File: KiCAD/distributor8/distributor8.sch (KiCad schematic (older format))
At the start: 52 parts, among them P1 CONN_02X03, P10 CONN_02X03, P11 CONN_02X03, P12 CONN_02X03, P13 CONN_02X03, P14 CONN_02X03, P15 CONN_02X03, P16 CONN_02X03, P17 CONN_02X03, P18 CONN_02X03, P19 CONN_02X03, P2 CONN_02X03, P20 CONN_02X03, P21 CONN_02X07, P22 CONN_02X07, P23 CONN_02X07, P24 CONN_02X07, P25 CONN_02X03, P26 CONN_02X03, P27 CONN_02X07, P28 CONN_02X07, P29 CONN_02X07, P3 CONN_02X03, P30 CONN_02X07, P31 CONN_02X03, P32 CONN_02X03, P33 CONN_02X03, P34 CONN_02X03, P35 CONN_02X07, P36 CONN_02X07, P37 CONN_02X07, P38 CONN_02X07, P39 CONN_02X03, P4 CONN_02X03, P40 CONN_02X03, P41 CONN_02X03, P42 CONN_02X03, P43 CONN_02X07, P44 CONN_02X07, P45 CONN_02X07, P46 CONN_02X07, P47 CONN_02X03, P48 CONN_02X03, P5 CONN_02X03, P6 CONN_02X03, P7 CONN_02X03, P8 CONN_02X03, P9 CONN_02X03

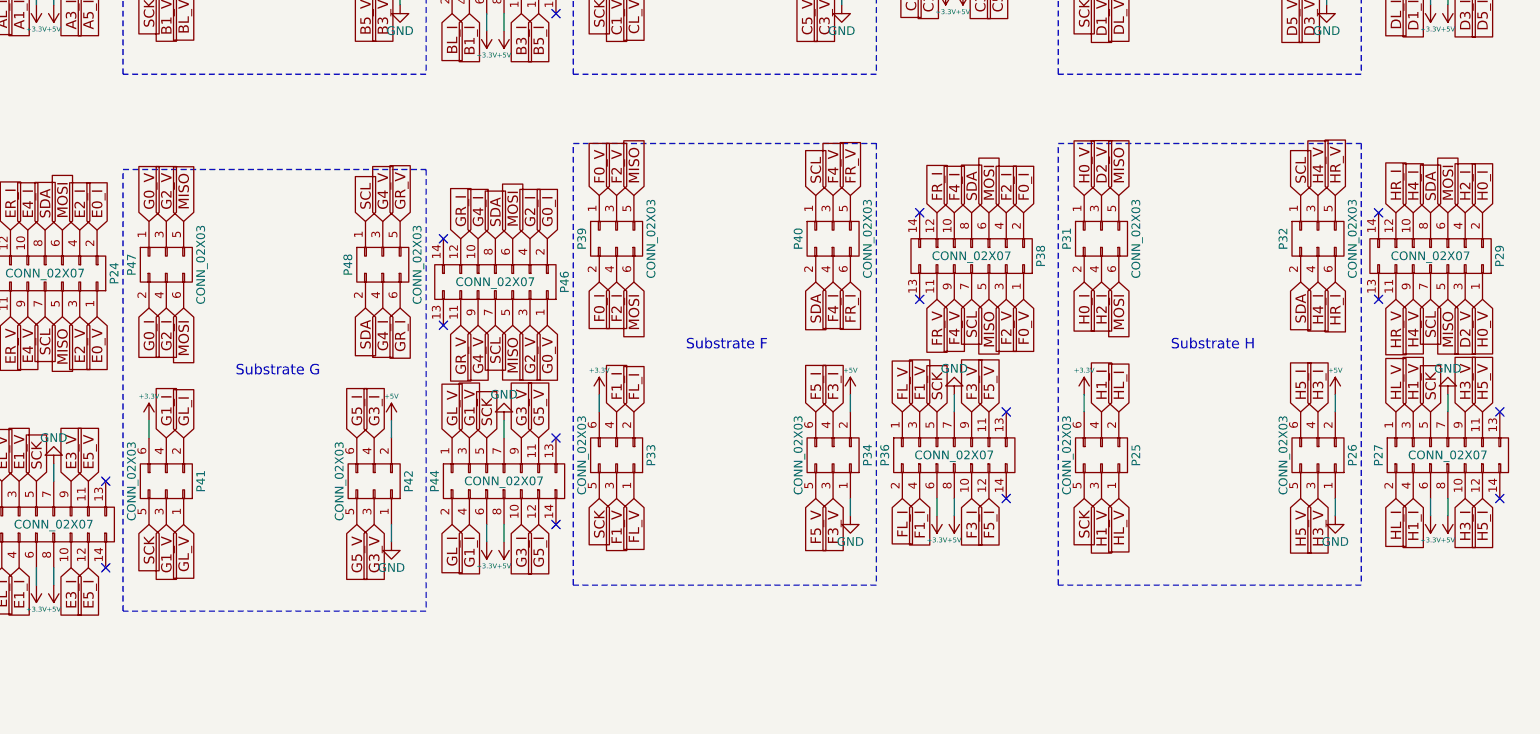
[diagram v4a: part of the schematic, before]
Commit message: try to fix messed up d8 routing
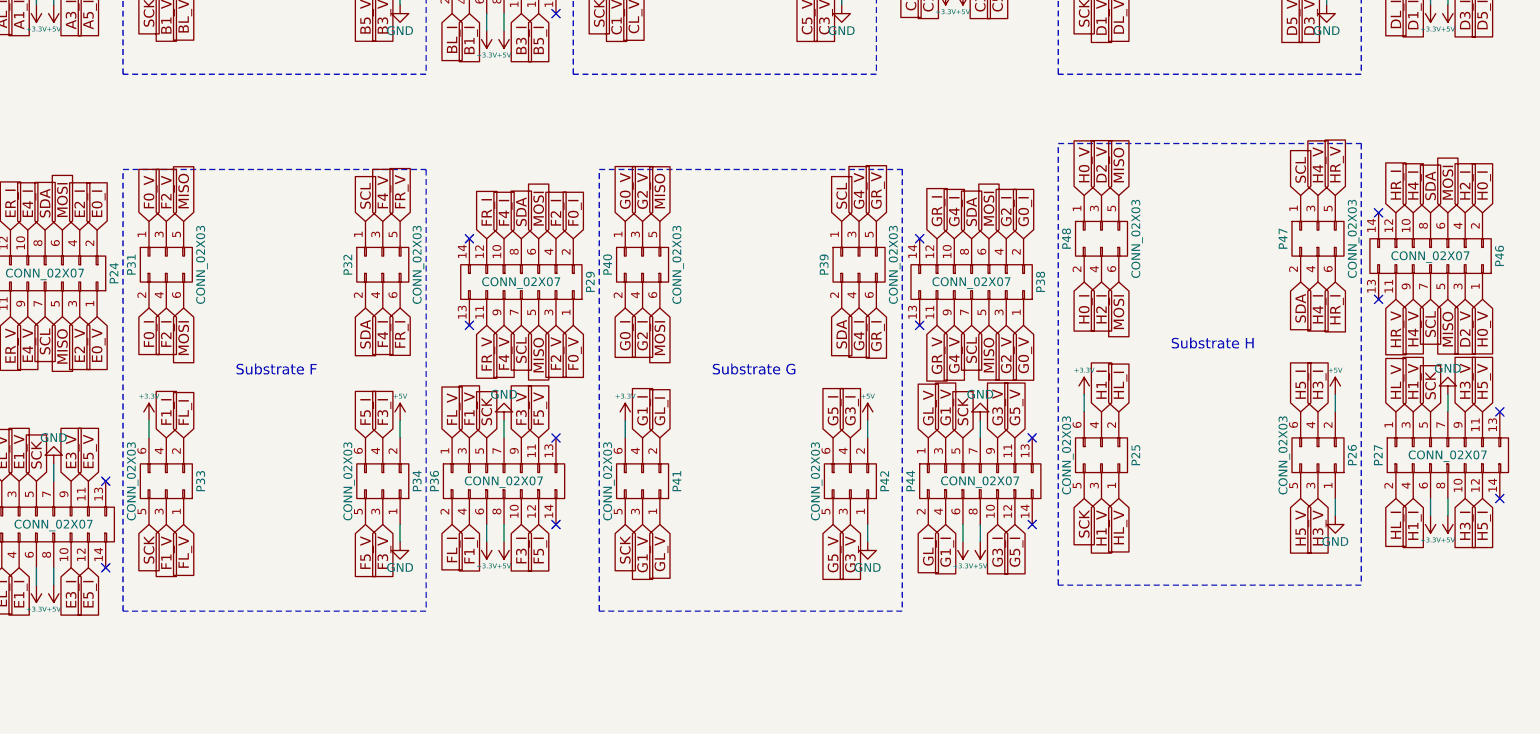
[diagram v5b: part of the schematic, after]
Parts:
- P40: renamed from P47; footprint myParts:SSW-107-02-T-D-RA -> myParts:TMS-103-01-L-D-SE
- renumbered P38 to P29, P39 to P31, P40 to P32, P46 to P38, P48 to P39, P29 to P46, P32 to P47, P31 to P48
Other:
- moved on the sheet: P29, P31, P32, P33, P34, P36, P38, P39, P40, P41, P42, P44

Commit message: fixed d8
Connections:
- net D2_V: no longer P46.3 (P3), P48.3 (P3)
- new net H2_V: P46.3 (P3), P48.3 (P3)
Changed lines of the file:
@@
 H0_V
 Text GLabel 8800 3800 1    60   Input ~ 0
-D2_V
+H2_V
 Text GLabel 10050 3800 1    60   Input ~ 0
 H4_V
@@
 H0_V
 Text GLabel 10900 4400 3    60   Input ~ 0
-D2_V
+H2_V
 Text GLabel 10800 4400 3    60   Input ~ 0
 MISO

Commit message: mux8 done
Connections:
- net +3V3 renamed CLK

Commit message: adding new spring pin boards
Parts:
- P21, P22, P23, P24, P27, P28, P29, P30, P35, P36, P37, P38, P43, P44, P45, P46: footprint myParts:SSW-107-02-T-D-RA -> myParts:SSW-106-02-T-D-RA-IN14
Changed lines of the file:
@@
 F 0 "P21" H 2750 2750 50  0000 C CNN
 F 1 "CONN_02X07" V 2750 2350 50  0000 C CNN
-F 2 "myParts:SSW-107-02-T-D-RA" H 2750 1150 50  0001 C CNN
+F 2 "myParts:SSW-106-02-T-D-RA-IN14" H 2750 1150 50  0001 C CNN
 F 3 "" H 2750 1150 50  0000 C CNN
 	1    2750 2350
@@
 F 0 "P23" H 2700 1600 50  0000 C CNN
 F 1 "CONN_02X07" V 2700 1200 50  0000 C CNN
-F 2 "myParts:SSW-107-02-T-D-RA" H 2700 0   50  0001 C CNN
+F 2 "myParts:SSW-106-02-T-D-RA-IN14" H 2700 0   50  0001 C CNN
 F 3 "" H 2700 0   50  0000 C CNN
 	1    2700 1200
@@
 F 0 "P28" H 5350 2900 50  0000 C CNN
 F 1 "CONN_02X07" V 5350 2500 50  0000 C CNN
-F 2 "myParts:SSW-107-02-T-D-RA" H 5350 1300 50  0001 C CNN
+F 2 "myParts:SSW-106-02-T-D-RA-IN14" H 5350 1300 50  0001 C CNN
 F 3 "" H 5350 1300 50  0000 C CNN
 	1    5350 2500
@@
 F 0 "P30" H 5300 1550 50  0000 C CNN
 F 1 "CONN_02X07" V 5300 1150 50  0000 C CNN
-F 2 "myParts:SSW-107-02-T-D-RA" H 5300 -50 50  0001 C CNN
+F 2 "myParts:SSW-106-02-T-D-RA-IN14" H 5300 -50 50  0001 C CNN
 F 3 "" H 5300 -50 50  0000 C CNN
 	1    5300 1150
@@
 F 0 "P35" H 8000 2650 50  0000 C CNN
 F 1 "CONN_02X07" V 8000 2250 50  0000 C CNN
-F 2 "myParts:SSW-107-02-T-D-RA" H 8000 1050 50  0001 C CNN
+F 2 "myParts:SSW-106-02-T-D-RA-IN14" H 8000 1050 50  0001 C CNN
 F 3 "" H 8000 1050 50  0000 C CNN
 	1    8000 2250
@@
 F 0 "P37" H 7900 1600 50  0000 C CNN
 F 1 "CONN_02X07" V 7900 1200 50  0000 C CNN
-F 2 "myParts:SSW-107-02-T-D-RA" H 7900 0   50  0001 C CNN
+F 2 "myParts:SSW-106-02-T-D-RA-IN14" H 7900 0   50  0001 C CNN
 F 3 "" H 7900 0   50  0000 C CNN
 	1    7900 1200
@@
 F 0 "P43" H 10800 2750 50  0000 C CNN
 F 1 "CONN_02X07" V 10800 2350 50  0000 C CNN
-F 2 "myParts:SSW-107-02-T-D-RA" H 10800 1150 50  0001 C CNN
+F 2 "myParts:SSW-106-02-T-D-RA-IN14" H 10800 1150 50  0001 C CNN
 F 3 "" H 10800 1150 50  0000 C CNN
 	1    10800 2350
@@
 F 0 "P45" H 10800 1600 50  0000 C CNN
 F 1 "CONN_02X07" V 10800 1200 50  0000 C CNN
-F 2 "myParts:SSW-107-02-T-D-RA" H 10800 0   50  0001 C CNN
+F 2 "myParts:SSW-106-02-T-D-RA-IN14" H 10800 0   50  0001 C CNN
 F 3 "" H 10800 0   50  0000 C CNN
 	1    10800 1200
@@
 F 0 "P22" H 2750 6100 50  0000 C CNN
 F 1 "CONN_02X07" V 2750 5700 50  0000 C CNN
-F 2 "myParts:SSW-107-02-T-D-RA" H 2750 4500 50  0001 C CNN
+F 2 "myParts:SSW-106-02-T-D-RA-IN14" H 2750 4500 50  0001 C CNN
 F 3 "" H 2750 4500 50  0000 C CNN
 	1    2750 5700
@@
 F 0 "P24" H 2700 4650 50  0000 C CNN
 F 1 "CONN_02X07" V 2700 4250 50  0000 C CNN
-F 2 "myParts:SSW-107-02-T-D-RA" H 2700 3050 50  0001 C CNN
+F 2 "myParts:SSW-106-02-T-D-RA-IN14" H 2700 3050 50  0001 C CNN
 F 3 "" H 2700 3050 50  0000 C CNN
 	1    2700 4250
@@
 F 0 "P27" H 10800 5700 50  0000 C CNN
 F 1 "CONN_02X07" V 10800 5300 50  0000 C CNN
-F 2 "myParts:SSW-107-02-T-D-RA" H 10800 4100 50  0001 C CNN
+F 2 "myParts:SSW-106-02-T-D-RA-IN14" H 10800 4100 50  0001 C CNN
 F 3 "" H 10800 4100 50  0000 C CNN
 	1    10800 5300
@@
 F 0 "P46" H 10700 4550 50  0000 C CNN
 F 1 "CONN_02X07" V 10700 4150 50  0000 C CNN
-F 2 "myParts:SSW-107-02-T-D-RA" H 10700 2950 50  0001 C CNN
+F 2 "myParts:SSW-106-02-T-D-RA-IN14" H 10700 2950 50  0001 C CNN
 F 3 "" H 10700 2950 50  0000 C CNN
 	1    10700 4150
@@
 F 0 "P36" H 5350 5850 50  0000 C CNN
 F 1 "CONN_02X07" V 5350 5450 50  0000 C CNN
-F 2 "myParts:SSW-107-02-T-D-RA" H 5350 4250 50  0001 C CNN
+F 2 "myParts:SSW-106-02-T-D-RA-IN14" H 5350 4250 50  0001 C CNN
 F 3 "" H 5350 4250 50  0000 C CNN
 	1    5350 5450
@@
 F 0 "P29" H 5450 4700 50  0000 C CNN
 F 1 "CONN_02X07" V 5450 4300 50  0000 C CNN
-F 2 "myParts:SSW-107-02-T-D-RA" H 5450 3100 50  0001 C CNN
+F 2 "myParts:SSW-106-02-T-D-RA-IN14" H 5450 3100 50  0001 C CNN
 F 3 "" H 5450 3100 50  0000 C CNN
 	1    5450 4300
@@
 F 0 "P44" H 8100 5850 50  0000 C CNN
 F 1 "CONN_02X07" V 8100 5450 50  0000 C CNN
-F 2 "myParts:SSW-107-02-T-D-RA" H 8100 4250 50  0001 C CNN
+F 2 "myParts:SSW-106-02-T-D-RA-IN14" H 8100 4250 50  0001 C CNN
 F 3 "" H 8100 4250 50  0000 C CNN
 	1    8100 5450
@@
 F 0 "P38" H 8050 4700 50  0000 C CNN
 F 1 "CONN_02X07" V 8050 4300 50  0000 C CNN
-F 2 "myParts:SSW-107-02-T-D-RA" H 8050 3100 50  0001 C CNN
+F 2 "myParts:SSW-106-02-T-D-RA-IN14" H 8050 3100 50  0001 C CNN
 F 3 "" H 8050 3100 50  0000 C CNN
 	1    8050 4300
